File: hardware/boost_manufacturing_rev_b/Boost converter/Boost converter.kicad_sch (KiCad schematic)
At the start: 39 parts, among them J1 Conn_01x02_Socket, J2 Conn_01x02_Socket, Q1 CSD18540Q5B, Q2 CSD18540Q5B, U1 LM5122QMHX/NOPB

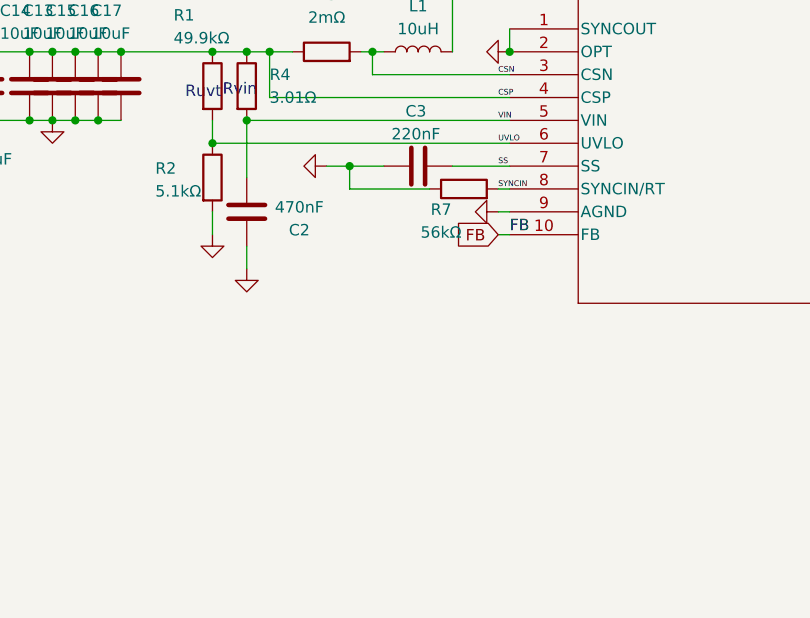
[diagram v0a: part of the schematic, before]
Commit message: hardware: refresh boost rev b outputs and add LM5050 OR-ing rev a package
Update Boost Converter Rev B design/manufacturing files and add a new LM5050 OR-ing manufacturing package with standardized documentation.

Boost Rev B:

- Updated KiCad source files (.kicad_sch/.kicad_pcb/.kicad_prl), symbol libraries, footprint library entries, and fp cache.

- Added MCU-controlled shutdown path by pulling LM5122 SS low via MOSFET.

- Kept UVLO path for threshold function (not used for shutdown), so each re-enable triggers a fresh soft-start ramp from SS release.

- Regenerated manufacturing artifacts: BOM, CPL, Gerbers, drill files, Gerber job, and Gerber.zip.

- Rotated project backup zips (removed older snapshots, added new snapshots).

- Updated Rev B README and bench test procedure to document SS-pull-down behavior and validation steps.

LM5050 OR-ing Rev A:

- Added new folder: hardware/lm5050_redundant_supply_manufacturing_rev_a following hardware naming conventions.

- Added KiCad project files, local libraries/footprints, BOM, CPL, Gerbers, Gerber.zip, and project backups for the High Side OR-ing board.

- Added standardized README and test_procedure_rev_a.md for bring-up and source switchover/reverse-blocking validation.

Repository docs and organization:

- Updated top-level README boost summary to include SS pull-down control and soft-start restart behavior.

- Moved rover software handoff doc to firmware/2026/rover-software-handoff.md and updated README references to the new path.
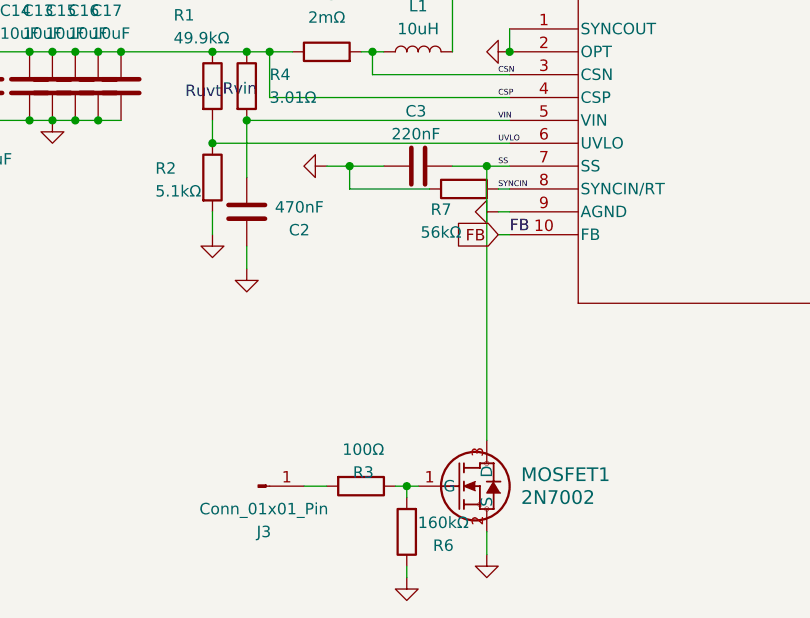
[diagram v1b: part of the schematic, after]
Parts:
- added J3: Conn_01x01_Pin, Connector_PinHeader_1.00mm:PinHeader_1x01_P1.00mm_Vertical, symbol Connector:Conn_01x01_Pin
- added MOSFET1: 2N7002, SOT-23TO-236_318-08_ONS, symbol Boost_Converter_Library:2N7002
- added R3: 100Ω, Resistor_SMD:R_0603_1608Metric, symbol Device:R
- added R6: 160kΩ, Resistor_SMD:R_0603_1608Metric, symbol Device:R
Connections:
- net GND: now also MOSFET1.2 (S), R6.1
- net SS: now also MOSFET1.3 (D)
- new net: MOSFET1.1 (G), R3.1, R6.2
- new net: J3.1 (Pin_1), R3.2
